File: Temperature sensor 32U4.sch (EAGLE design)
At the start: 30 parts, among them IC1 ATMEGA32U4-AU, IC2 LM2940CS-5.0_NOPB, T1 BD139, X1 16MHz

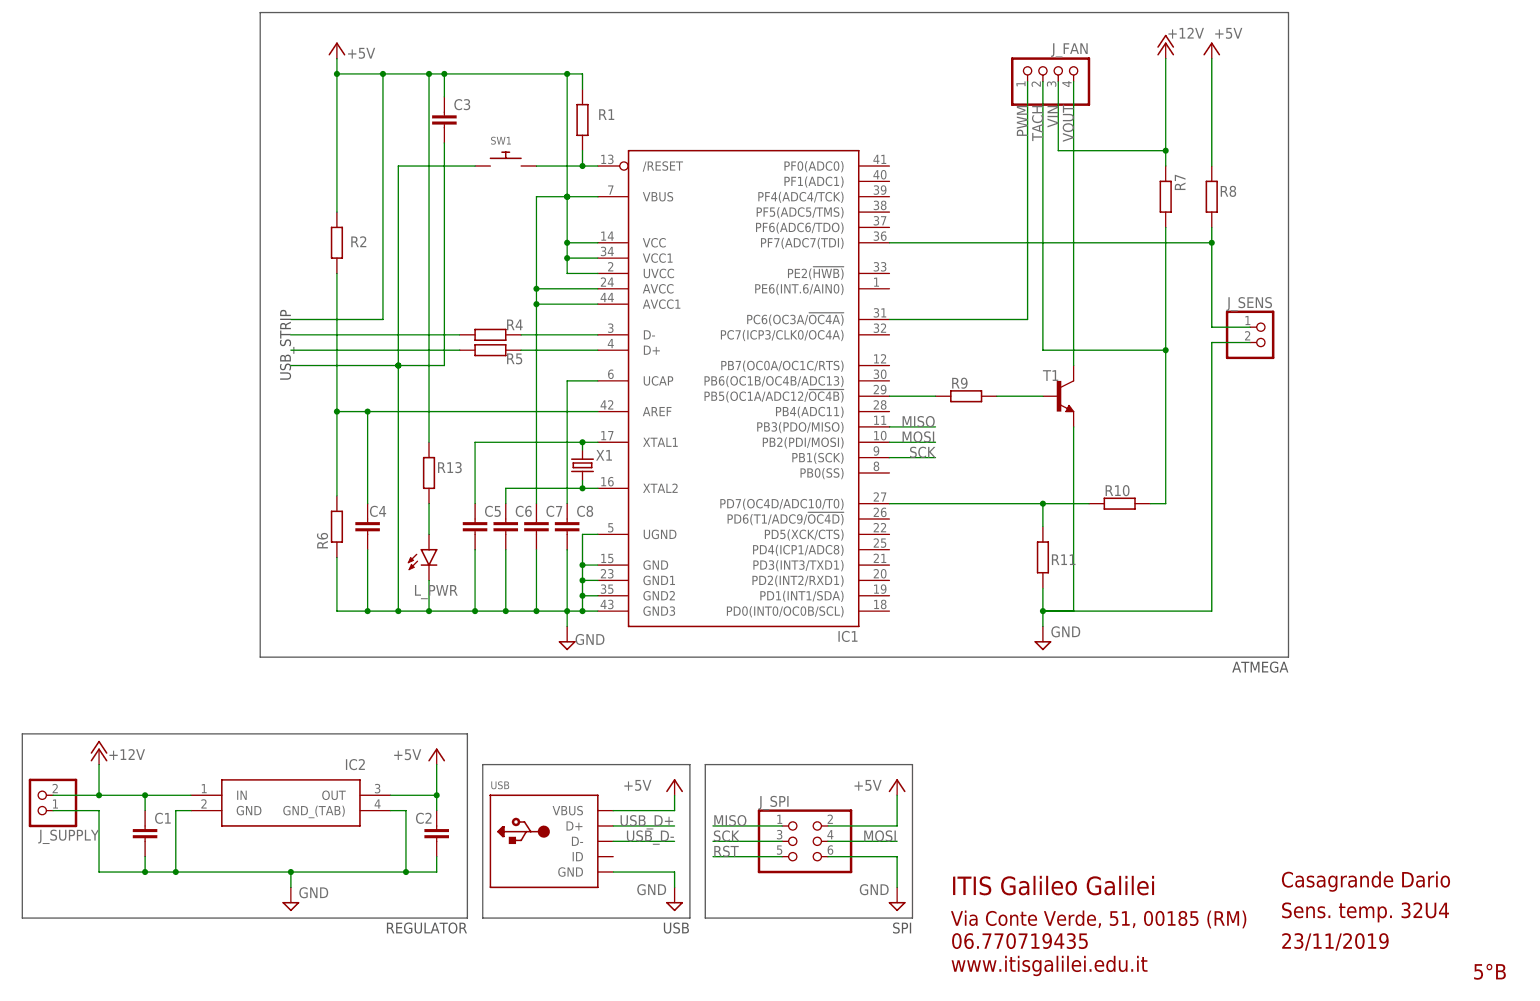
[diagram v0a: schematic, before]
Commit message: Fixed schematic and deleted backup files
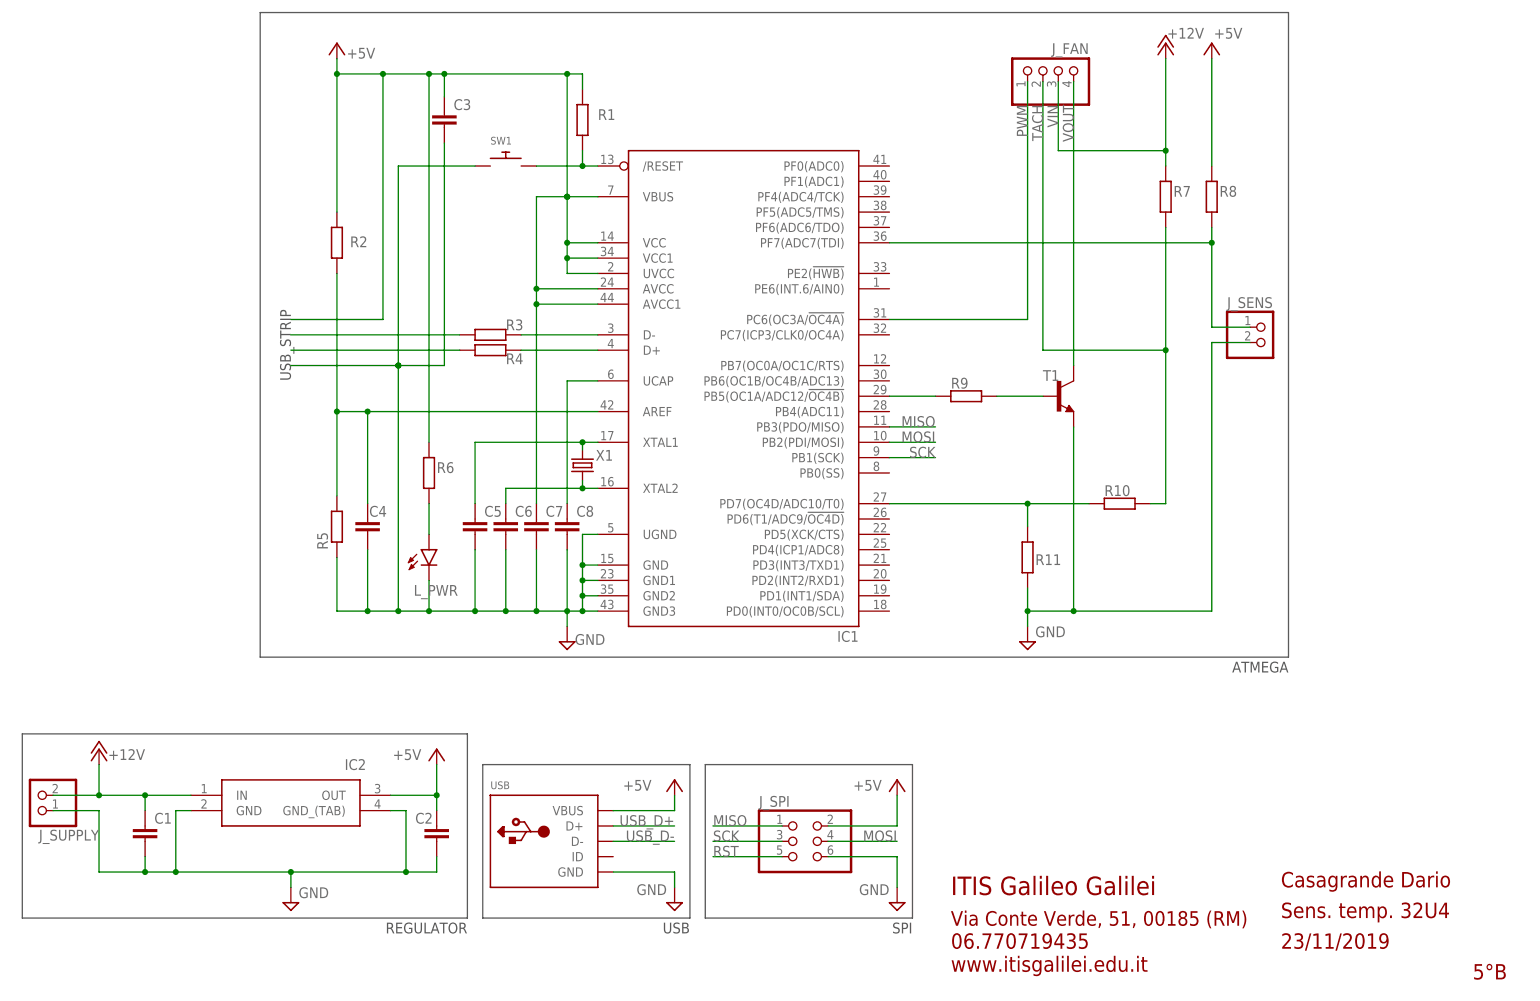
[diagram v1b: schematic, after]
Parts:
- removed R13: 270, rcl:R-EU_R1206
- added R3: 10, rcl:R-EU_R1206
- R5: value 10 -> 8,2k
- R6: value 8,2k -> 270
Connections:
- net +5V: now also R6.1; no longer R13.1
- net AREF: now also R5.2; no longer R6.2
- net D+: now also R4.1; no longer R5.1
- net D-: now also R3.1; no longer R4.1
- net GND: now also R5.1; no longer R6.1
- net N$1: now also R6.2; no longer R13.2
- net USB_D+: now also R4.2; no longer R5.2
- net USB_D-: now also R3.2; no longer R4.2
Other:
- moved on the sheet: R11, R4, R5, R6
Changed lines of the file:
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@@
 <setting verticaltext="up"/>
 </settings>
-<grid distance="0.1" unitdist="inch" unit="inch" style="lines" multiple="1" display="no" altdistance="0.01" altunitdist="inch" altunit="inch"/>
+<grid distance="0.1" unitdist="inch" unit="inch" style="lines" multiple="1" display="yes" altdistance="0.05" altunitdist="inch" altunit="inch"/>
 <layers>
 <layer number="1" name="Top" color="4" fill="1" visible="no" active="no"/>
@@
 <part name="C6" library="rcl" library_urn="urn:adsk.eagle:library:334" deviceset="C-EU" device="C1206" package3d_urn="urn:adsk.eagle:package:23618/2" value="22p"/>
 <part name="R1" library="rcl" library_urn="urn:adsk.eagle:library:334" deviceset="R-EU_" device="R1206" package3d_urn="urn:adsk.eagle:package:23540/2" value="10k"/>
+<part name="R3" library="rcl" library_urn="urn:adsk.eagle:library:334" deviceset="R-EU_" device="R1206" package3d_urn="urn:adsk.eagle:package:23540/2" value="10"/>
 <part name="R4" library="rcl" library_urn="urn:adsk.eagle:library:334" deviceset="R-EU_" device="R1206" package3d_urn="urn:adsk.eagle:package:23540/2" value="10"/>
-<part name="R5" library="rcl" library_urn="urn:adsk.eagle:library:334" deviceset="R-EU_" device="R1206" package3d_urn="urn:adsk.eagle:package:23540/2" value="10"/>
 <part name="T1" library="transistor" library_urn="urn:adsk.eagle:library:402" deviceset="BD139" device="" package3d_urn="urn:adsk.eagle:package:29898/1"/>
 <part name="R9" library="rcl" library_urn="urn:adsk.eagle:library:334" deviceset="R-EU_" device="R1206" package3d_urn="urn:adsk.eagle:package:23540/2" value="150"/>
@@
 <part name="R11" library="rcl" library_urn="urn:adsk.eagle:library:334" deviceset="R-EU_" device="R1206" package3d_urn="urn:adsk.eagle:package:23540/2" value="14k"/>
 <part name="R2" library="rcl" library_urn="urn:adsk.eagle:library:334" deviceset="R-EU_" device="R1206" package3d_urn="urn:adsk.eagle:package:23540/2" value="1,8k"/>
-<part name="R6" library="rcl" library_urn="urn:adsk.eagle:library:334" deviceset="R-EU_" device="R1206" package3d_urn="urn:adsk.eagle:package:23540/2" value="8,2k"/>
+<part name="R5" library="rcl" library_urn="urn:adsk.eagle:library:334" deviceset="R-EU_" device="R1206" package3d_urn="urn:adsk.eagle:package:23540/2" value="8,2k"/>
 <part name="C4" library="rcl" library_urn="urn:adsk.eagle:library:334" deviceset="C-EU" device="C1206" package3d_urn="urn:adsk.eagle:package:23618/2" value="1u"/>
 <part name="R8" library="rcl" library_urn="urn:adsk.eagle:library:334" deviceset="R-EU_" device="R1206" package3d_urn="urn:adsk.eagle:package:23540/2" value="10k"/>
@@
 <part name="GND4" library="supply2" library_urn="urn:adsk.eagle:library:372" deviceset="GND" device=""/>
 <part name="L_PWR" library="led" library_urn="urn:adsk.eagle:library:259" deviceset="LED" device="CHIPLED_1206" package3d_urn="urn:adsk.eagle:package:15823/2"/>
-<part name="R13" library="rcl" library_urn="urn:adsk.eagle:library:334" deviceset="R-EU_" device="R1206" package3d_urn="urn:adsk.eagle:package:23540/2" value="270"/>
+<part name="R6" library="rcl" library_urn="urn:adsk.eagle:library:334" deviceset="R-EU_" device="R1206" package3d_urn="urn:adsk.eagle:package:23540/2" value="270"/>
 <part name="SUPPLY1" library="supply2" library_urn="urn:adsk.eagle:library:372" deviceset="GND" device=""/>
 <part name="IC2" library="LM2940CS-5.0_NOPB" deviceset="LM2940CS-5.0_NOPB" device=""/>
@@
 <attribute name="NAME" x="104.14" y="147.32" size="1.778" layer="95"/>
 </instance>
-<instance part="R4" gate="G$1" x="86.36" y="111.76" smashed="yes" rot="R180">
+<instance part="R3" gate="G$1" x="86.36" y="111.76" smashed="yes" rot="R180">
 <attribute name="NAME" x="88.9" y="114.3" size="1.778" layer="95" rot="MR180"/>
 </instance>
-<instance part="R5" gate="G$1" x="86.36" y="109.22" smashed="yes" rot="R180">
+<instance part="R4" gate="G$1" x="86.36" y="109.22" smashed="yes" rot="R180">
 <attribute name="NAME" x="88.9" y="106.9086" size="1.778" layer="95"/>
 </instance>
@@
 <attribute name="NAME" x="185.42" y="160.02" size="1.778" layer="95" rot="R180"/>
 </instance>
-<instance part="GND3" gate="GND" x="177.8" y="60.96" smashed="yes">
-<attribute name="VALUE" x="179.07" y="63.5" size="1.778" layer="96" rot="MR180"/>
+<instance part="GND3" gate="GND" x="175.26" y="60.96" smashed="yes">
+<attribute name="VALUE" x="176.53" y="63.5" size="1.778" layer="96" rot="MR180"/>
 </instance>
 <instance part="P+3" gate="1" x="198.12" y="160.02" smashed="yes">
@@
 </instance>
 <instance part="R7" gate="G$1" x="198.12" y="134.62" smashed="yes" rot="R270">
-<attribute name="NAME" x="199.6186" y="138.43" size="1.778" layer="95" rot="R270"/>
+<attribute name="NAME" x="199.39" y="134.62" size="1.778" layer="95"/>
 </instance>
 <instance part="R10" gate="G$1" x="190.5" y="83.82" smashed="yes" rot="R180">
 <attribute name="NAME" x="187.96" y="85.09" size="1.778" layer="95"/>
 </instance>
-<instance part="R11" gate="G$1" x="177.8" y="74.93" smashed="yes" rot="R270">
-<attribute name="NAME" x="179.07" y="73.66" size="1.778" layer="95"/>
+<instance part="R11" gate="G$1" x="175.26" y="74.93" smashed="yes" rot="R270">
+<attribute name="NAME" x="176.53" y="73.66" size="1.778" layer="95"/>
 </instance>
 <instance part="R2" gate="G$1" x="60.96" y="127" smashed="yes" rot="R90">
 <attribute name="NAME" x="66.04" y="128.0414" size="1.778" layer="95" rot="R180"/>
 </instance>
-<instance part="R6" gate="G$1" x="60.96" y="80.01" smashed="yes" rot="R90">
+<instance part="R5" gate="G$1" x="60.96" y="80.01" smashed="yes" rot="R90">
 <attribute name="NAME" x="59.4614" y="76.2" size="1.778" layer="95" rot="R90"/>
 </instance>
@@
 <attribute name="VALUE" x="81.915" y="71.628" size="1.778" layer="96" rot="R90"/>
 </instance>
-<instance part="R13" gate="G$1" x="76.2" y="88.9" smashed="yes" rot="R270">
+<instance part="R6" gate="G$1" x="76.2" y="88.9" smashed="yes" rot="R270">
 <attribute name="NAME" x="77.47" y="88.9" size="1.778" layer="95"/>
 </instance>
@@
 </segment>
 <segment>
-<pinref part="R6" gate="G$1" pin="1"/>
+<pinref part="R5" gate="G$1" pin="1"/>
 <wire x1="60.96" y1="74.93" x2="60.96" y2="66.04" width="0.1524" layer="91"/>
 <pinref part="IC1" gate="G$1" pin="UGND"/>
@@
 <segment>
 <pinref part="R11" gate="G$1" pin="2"/>
-<wire x1="177.8" y1="69.85" x2="177.8" y2="66.04" width="0.1524" layer="91"/>
-<wire x1="182.88" y1="66.04" x2="177.8" y2="66.04" width="0.1524" layer="91"/>
-<pinref part="T1" gate="G$1" pin="E"/>
-<wire x1="182.88" y1="66.04" x2="182.88" y2="96.52" width="0.1524" layer="91"/>
-<junction x="177.8" y="66.04"/>
-<wire x1="205.74" y1="66.04" x2="177.8" y2="66.04" width="0.1524" layer="91"/>
+<wire x1="175.26" y1="69.85" x2="175.26" y2="66.04" width="0.1524" layer="91"/>
+<junction x="175.26" y="66.04"/>
+<wire x1="205.74" y1="66.04" x2="182.88" y2="66.04" width="0.1524" layer="91"/>
 <pinref part="J_SENS" gate="G$1" pin="2"/>
+<wire x1="182.88" y1="66.04" x2="175.26" y2="66.04" width="0.1524" layer="91"/>
 <wire x1="205.74" y1="110.49" x2="205.74" y2="66.04" width="0.1524" layer="91"/>
 <wire x1="212.09" y1="110.49" x2="205.74" y2="110.49" width="0.1524" layer="91"/>
 <pinref part="GND3" gate="GND" pin="GND"/>
-<wire x1="177.8" y1="63.5" x2="177.8" y2="66.04" width="0.1524" layer="91"/>
+<wire x1="175.26" y1="63.5" x2="175.26" y2="66.04" width="0.1524" layer="91"/>
+<pinref part="T1" gate="G$1" pin="E"/>
+<wire x1="182.88" y1="96.52" x2="182.88" y2="66.04" width="0.1524" layer="91"/>
+<junction x="182.88" y="66.04"/>
 </segment>
 </net>
@@
 <wire x1="104.14" y1="134.62" x2="99.06" y2="134.62" width="0.1524" layer="91"/>
 <junction x="99.06" y="134.62"/>
-<pinref part="R13" gate="G$1" pin="1"/>
+<pinref part="R6" gate="G$1" pin="1"/>
 <wire x1="76.2" y1="93.98" x2="76.2" y2="154.94" width="0.1524" layer="91"/>
 <junction x="76.2" y="154.94"/>
@@
 <net name="USB_D-" class="0">
 <segment>
-<pinref part="R4" gate="G$1" pin="2"/>
+<pinref part="R3" gate="G$1" pin="2"/>
 <wire x1="53.34" y1="111.76" x2="81.28" y2="111.76" width="0.1524" layer="91"/>
 </segment>
@@
 <net name="D-" class="0">
 <segment>
-<pinref part="R4" gate="G$1" pin="1"/>
+<pinref part="R3" gate="G$1" pin="1"/>
 <pinref part="IC1" gate="G$1" pin="D-"/>
 <wire x1="91.44" y1="111.76" x2="104.14" y2="111.76" width="0.1524" layer="91"/>
@@
 <net name="USB_D+" class="0">
 <segment>
-<pinref part="R5" gate="G$1" pin="2"/>
+<pinref part="R4" gate="G$1" pin="2"/>
 <wire x1="53.34" y1="109.22" x2="81.28" y2="109.22" width="0.1524" layer="91"/>
 </segment>
@@
 <net name="D+" class="0">
 <segment>
-<pinref part="R5" gate="G$1" pin="1"/>
+<pinref part="R4" gate="G$1" pin="1"/>
 <pinref part="IC1" gate="G$1" pin="D+"/>
 <wire x1="91.44" y1="109.22" x2="104.14" y2="109.22" width="0.1524" layer="91"/>
@@
 <segment>
 <pinref part="R2" gate="G$1" pin="1"/>
-<pinref part="R6" gate="G$1" pin="2"/>
+<pinref part="R5" gate="G$1" pin="2"/>
 <wire x1="60.96" y1="121.92" x2="60.96" y2="99.06" width="0.1524" layer="91"/>
 <pinref part="IC1" gate="G$1" pin="AREF"/>
@@
 <pinref part="R10" gate="G$1" pin="2"/>
 <pinref part="R11" gate="G$1" pin="1"/>
-<wire x1="177.8" y1="80.01" x2="177.8" y2="83.82" width="0.1524" layer="91"/>
+<wire x1="175.26" y1="80.01" x2="175.26" y2="83.82" width="0.1524" layer="91"/>
 <pinref part="IC1" gate="G$1" pin="PD7(OC4D/ADC10/T0)"/>
-<wire x1="177.8" y1="83.82" x2="185.42" y2="83.82" width="0.1524" layer="91"/>
-<wire x1="152.4" y1="83.82" x2="177.8" y2="83.82" width="0.1524" layer="91"/>
-<junction x="177.8" y="83.82"/>
+<wire x1="175.26" y1="83.82" x2="185.42" y2="83.82" width="0.1524" layer="91"/>
+<wire x1="152.4" y1="83.82" x2="175.26" y2="83.82" width="0.1524" layer="91"/>
+<junction x="175.26" y="83.82"/>
 </segment>
 </net>
 <net name="N$1" class="0">
 <segment>
-<pinref part="R13" gate="G$1" pin="2"/>
+<pinref part="R6" gate="G$1" pin="2"/>
 <pinref part="L_PWR" gate="G$1" pin="A"/>
 <wire x1="76.2" y1="83.82" x2="76.2" y2="78.74" width="0.1524" layer="91"/>

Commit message: Replaced BJT with a MOSFET
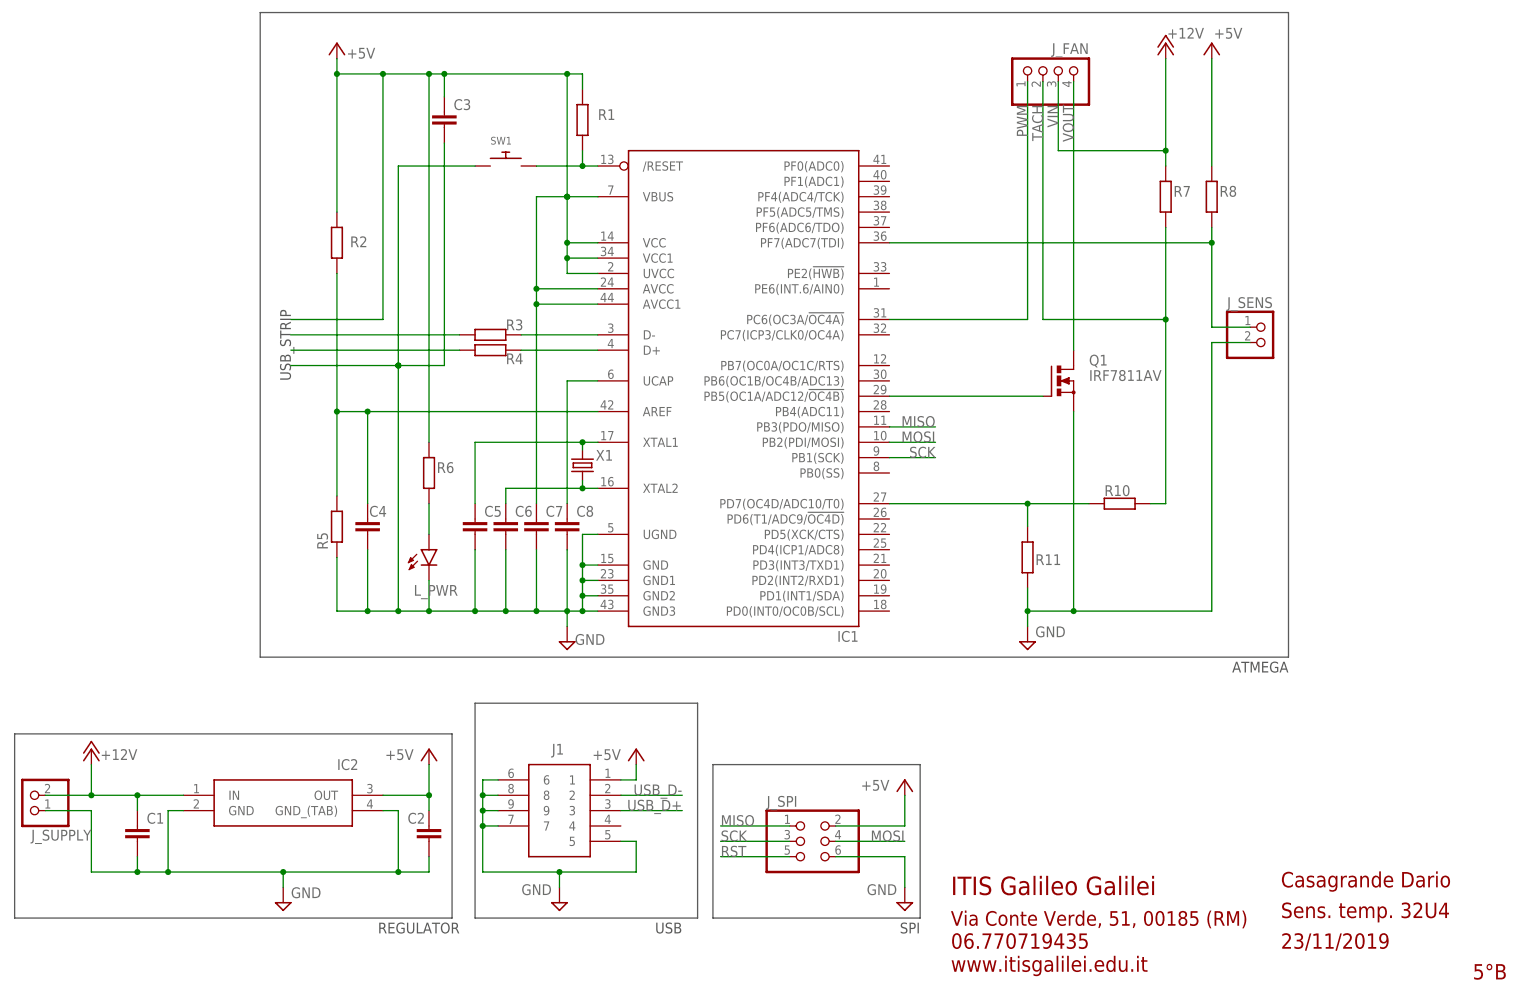
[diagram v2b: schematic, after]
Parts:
- removed R9: 150, rcl:R-EU_R1206
- removed T1: BD139, transistor:BD139
- removed USB: (no value), adafruit:USBMINIB
- added J1: 10104111-0001LF, USB:10104111-0001LF
- added Q1: IRF7811AV, transistor-power:N-MOSFET-SO8S
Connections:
- removed net FANSW: IC1.PB5(OC1A/ADC12/!OC4B), R9.2
- net +5V: now also J1.1; no longer USB.VBUS
- net GND: now also J1.5, J1.6, J1.7, J1.8, J1.9, Q1.S; no longer T1.E, USB.GND
- net N$2: now also IC1.PB5(OC1A/ADC12/!OC4B), Q1.G; no longer R9.1, T1.B
- net USB_D+: now also J1.3; no longer USB.D+
- net USB_D-: now also J1.2; no longer USB.D-
- net VOUT: now also Q1.D; no longer T1.C
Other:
- moved on the sheet: C1, C2, IC2, J_SPI, J_SUPPLY
